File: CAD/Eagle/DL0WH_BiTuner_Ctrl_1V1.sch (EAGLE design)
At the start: 141 parts, among them Q0321 ABS07-32.768KHZ, U0101 STM32L476RXT_64PIN_LDO, U0601 MC33996, U0701 MC33996, U0801 MC33996, U0921 TS5A23166, U0951 OPA354, U1001 MAX232_SOIC16, U1101 MAX232_SOIC16, U1201 LM53603-Q1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

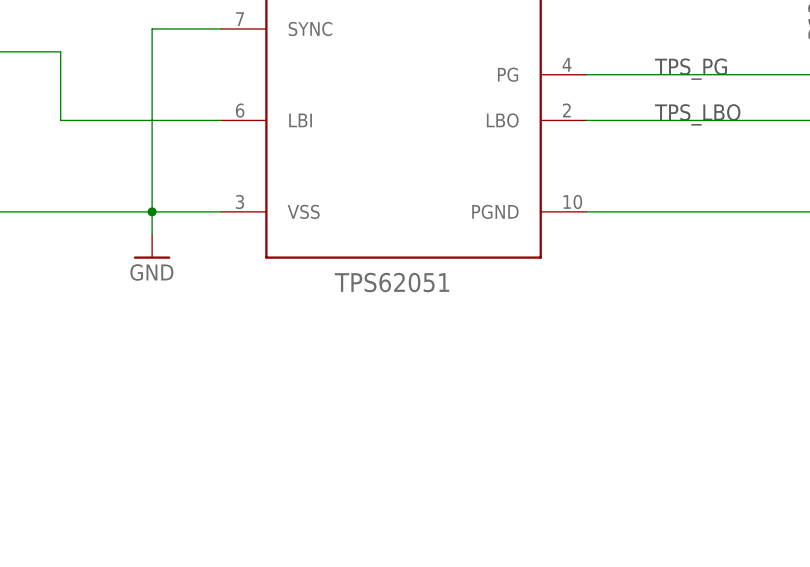
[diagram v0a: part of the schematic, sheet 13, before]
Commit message: HW_1V0 HW_1V1 HW_1V2 - TPS62051 changed to TPS62056
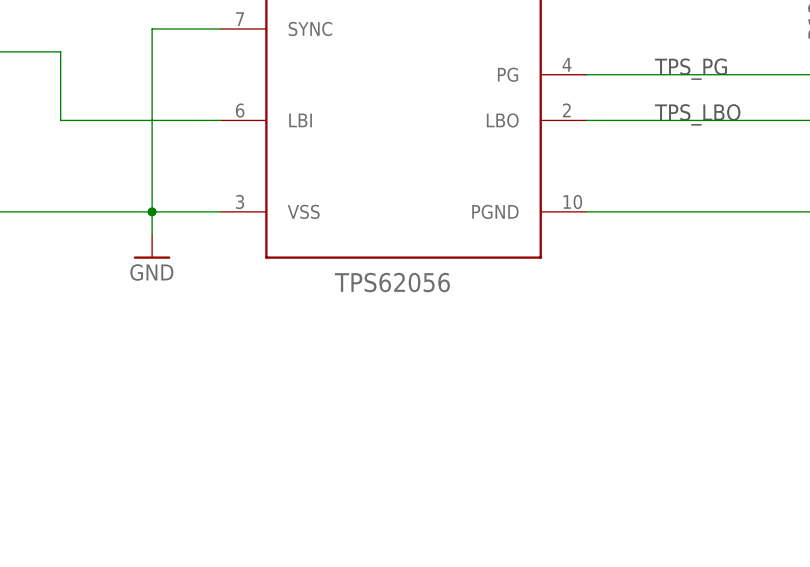
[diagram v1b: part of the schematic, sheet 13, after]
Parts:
- U1301: value TPS62051 -> TPS62056
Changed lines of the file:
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@@
 <part name="R0724" library="df4iah_rcl" deviceset="R-EU_" device="R0402" value="47R"/>
 <part name="R0824" library="df4iah_rcl" deviceset="R-EU_" device="R0402" value="47R"/>
-<part name="U1301" library="df4iah_powersupply" deviceset="TPS62051" device=""/>
+<part name="U1301" library="df4iah_powersupply" deviceset="TPS62051" device="" value="TPS62056"/>
 <part name="L1311" library="df4iah_rcl" deviceset="L-EU" device="4.50X3.20MM" value="10uH"/>
 <part name="R1321" library="df4iah_rcl" deviceset="R-EU_" device="R0402" value="1MR"/>
